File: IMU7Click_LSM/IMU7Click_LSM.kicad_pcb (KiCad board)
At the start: 2 copper layers, 28.8 x 29.2 mm, 13 parts, among them Q1 NMOS, U2 ICM-42688-P

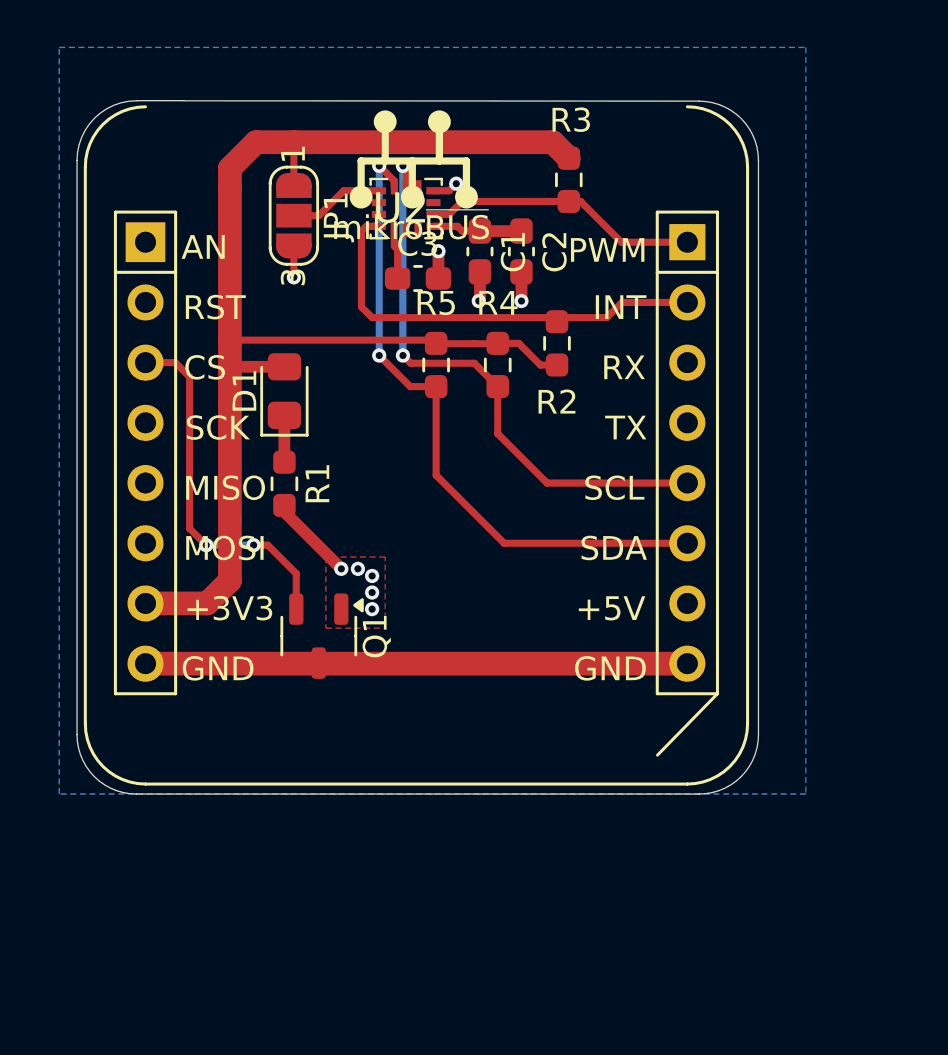
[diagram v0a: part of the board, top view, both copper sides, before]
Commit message: started st imu board
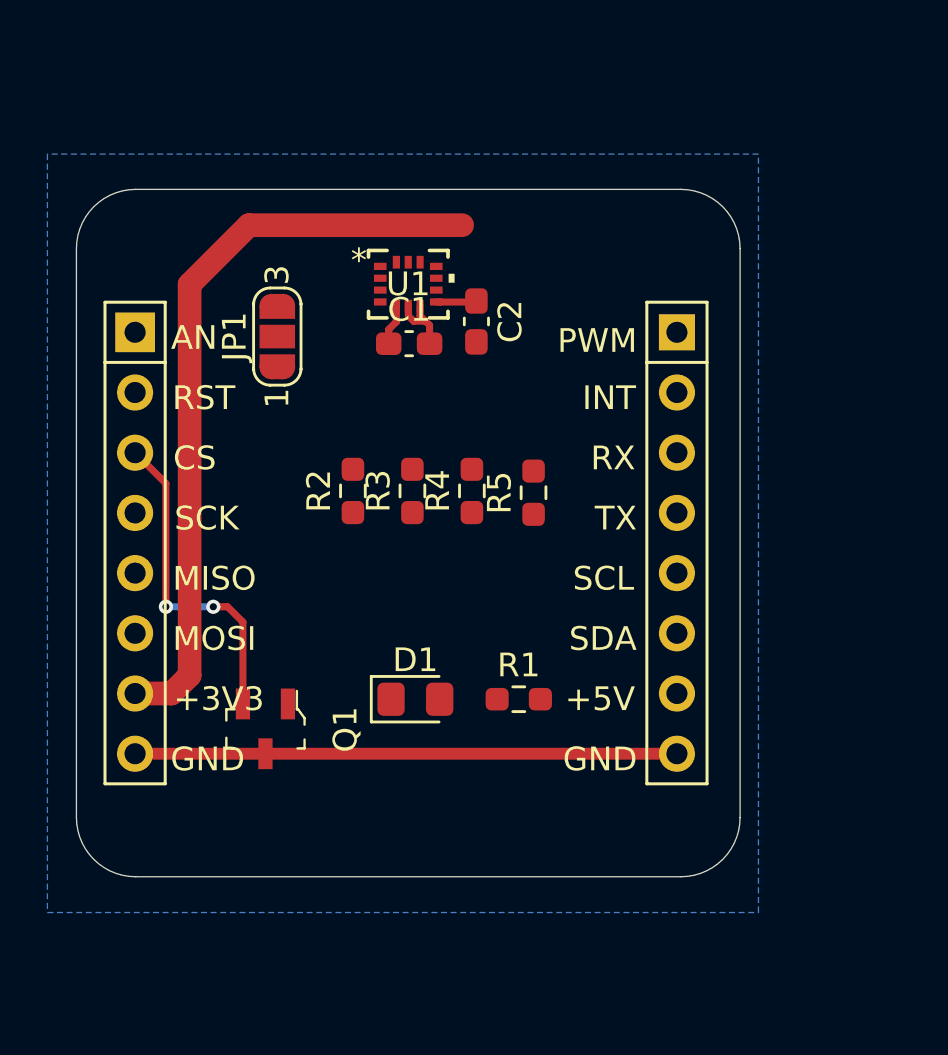
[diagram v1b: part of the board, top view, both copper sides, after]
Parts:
- removed C3: 10nF, Capacitor_SMD:C_0603_1608Metric_Pad1.08x0.95mm_HandSolder
- C2: value 2uF2 -> 100nF
- Q1: footprint Package_TO_SOT_SMD:SOT-23-3 -> digikey-footprints:SOT-23-3
- U1: value ~ -> LSM6DSV; footprint mikroBUS:MIKROBUS_HOST_CONN -> LSM6DSV:LGA14-L_2P59X3P1X0P5_STM
- U2: value ICM-42688-P -> ~; footprint ICM-42688-P:ICM-42688-P -> mikroBUS:MIKROBUS_HOST_CONN
- moved R3 14.7 mm to (134.2, 83.7), turned to 90 degrees
- moved D1 14.1 mm to (134.3, 92.5), turned to 0 degrees
- moved R1 13.4 mm to (138.7, 92.5), turned to 0 degrees
- moved U2 12.6 mm to (122.5, 77.0)
- moved U1 11.2 mm to (134.0, 75.0)
- moved R2 10.6 mm to (131.7, 83.7)
- moved R5 6.78 mm to (139.3, 83.8), turned to 90 degrees
- moved R4 5.42 mm to (136.7, 83.7), turned to 90 degrees
- moved JP1 5.15 mm to (128.5, 77.2), turned to 90 degrees
- moved C1 4.90 mm to (134.0, 77.5), turned to 0 degrees
- moved Q1 4.51 mm to (128.0, 93.8)
- moved C2 3.51 mm to (136.9, 76.6)
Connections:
- D1 pad 1: Net-(D1-K) -> GND1
- D1 pad 2: +3V3 -> Net-(D1-A)
- JP1 pad 2: Net-(JP1-C) -> /SA0
- R1 pad 1: Net-(D1-K) -> +3V3
- R1 pad 2: GND1 -> Net-(D1-A)
- R2 pad 2: Net-(U1B-INT1) -> /INT_2
- R3 pad 2: Net-(U1B-PWM) -> /INT_1
- R4 pad 2: /I2C_SCL -> /I2CS_SDA
- R5 pad 2: /I2C_SDA -> /I2CS_SDA
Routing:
- net /I2C_SDA: track 27.6 -> 0.00 mm, vias 2 -> 0
- net +3V3: track 61.0 -> 35.1 mm
- net /I2C_SCL: track 24.3 -> 0.00 mm, vias 2 -> 0
- net Net-(U1B-INT1): track 18.2 -> 0.00 mm
- net Net-(U1B-PWM): track 11.7 -> 0.00 mm
- net GND1: track 9.68 -> 2.97 mm, vias 10 -> 0
- net Net-(JP1-C): track 4.02 -> 0.00 mm
- net Net-(D1-K): track 1.98 -> 0.00 mm
- net /IMU_EN: track 15.4 -> 14.0 mm
- removed copper zone on F.Cu, net GND1
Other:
- board size 28.8 x 29.2 mm -> 28 x 29 mm
